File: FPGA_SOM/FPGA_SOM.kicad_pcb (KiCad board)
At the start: 6 copper layers, 49 x 47.1 mm, 64 parts, among them J1 Conn_01x12, J2 Conn_02x05_Counter_Clockwise, J3 Conn_01x06, J5 Conn_01x02, J7 Conn_01x09, J8 Conn_01x10, SW1 SW_Push, U1 ICE40UP5K-SG48ITR, U2 AP2127N-3.3, U3 AP2127N-1.2, U4 W25X20CLSN, X1 ECS-2520MV-xxx-xx

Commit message: QOL changes before production.
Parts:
- removed the ? at (147.2, 112.8) (x2)
- removed the ? at (147.5, 140.8)
- removed D2, D3, D4: LED_Small, Diode_SMD:D_0603_1608Metric_Pad1.05x0.95mm_HandSolder
- removed TP5: FSS, TestPoint:TestPoint_THTPad_D2.0mm_Drill1.0mm
- removed TP6: ISS, TestPoint:TestPoint_THTPad_D2.0mm_Drill1.0mm
- added ?: , , F.Cu at (197.2, 98.8)
- added ?: , , F.Cu at (158.5, 62.1)
- added ?: , , B.Cu at (197.2, 98.8)
- added ?: , , B.Cu at (197.2, 70.9)
- added ?: , , B.Cu at (158.5, 62.1)
- added D1: LED_RAGB, LED_SMD:LED_SK6812_EC15_1.5x1.5mm, F.Cu at (182.4, 70.5)
- added R14: 2k2, Resistor_SMD:R_0603_1608Metric, F.Cu at (183.9, 75.8)
- added R15: 2k2, Resistor_SMD:R_0603_1608Metric, F.Cu at (182.4, 75.8)
- added R16: 2k2, Resistor_SMD:R_0603_1608Metric, F.Cu at (180.6, 75.8)
- C17, C7: footprint Capacitor_SMD:C_0805_2012Metric -> Capacitor_SMD:C_0603_1608Metric
- FB1: footprint Resistor_SMD:R_1206_3216Metric -> Resistor_SMD:R_0603_1608Metric
- X1: value ECS-2520MV-xxx-xx -> SX2M20.000B10F20TNN
- moved REF** 85.2 mm to (197.1, 71.5)
- moved R11 68.4 mm to (167.3, 91.7)
- moved FB1 65.7 mm to (172.1, 71.4)
- moved C17 65.3 mm to (172.1, 73.5)
- moved C1 65.2 mm to (180.6, 81.5)
- moved C2 65.2 mm to (180.6, 81.5)
- moved C3 65.2 mm to (177.1, 88.6)
- moved J1 65.2 mm to (189.6, 62.2)
- moved J5 65.2 mm to (170.1, 89.0)
- moved R6 65.2 mm to (173.4, 91.1)
- moved TP9 65.2 mm to (167.8, 96.8)
- moved C12 65.2 mm to (168.5, 82.3)
- moved C18 65.2 mm to (175.5, 71.3)
- moved C20 65.2 mm to (177.0, 93.1)
- moved C5 65.2 mm to (168.5, 80.3)
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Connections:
- REF** pad 1: GND -> /3V3
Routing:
- net +5V: track 7.72 -> 14.9 mm, vias 0 -> 3
- net /ICE_SS: track 15.1 -> 9.36 mm
- net Net-(D1-GK): track 0.00 -> 5.20 mm
- net Net-(D1-BK): track 0.00 -> 4.65 mm
- net Net-(D1-RK): track 0.00 -> 4.51 mm
- net /FLASH_SS: track 23.5 -> 20.1 mm
- net /3V3: track 14.9 -> 13.4 mm, vias 23 -> 21
- net /3: track 22.6 -> 23.8 mm
- net /11: track 23.7 -> 23.0 mm, vias 1 -> 0
- net GND: vias 160 -> 94
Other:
- board text added: "JLCJLCJLCJLC"
- board text added: "NCGND 3V3 CDN ~{CRST} NC SCK FDI FDO FSS"
- board text removed: "Git Repo"
- board text removed: "NC GND 3V3 CDN ~{CRST} NC SCK FDI FDO FSS"

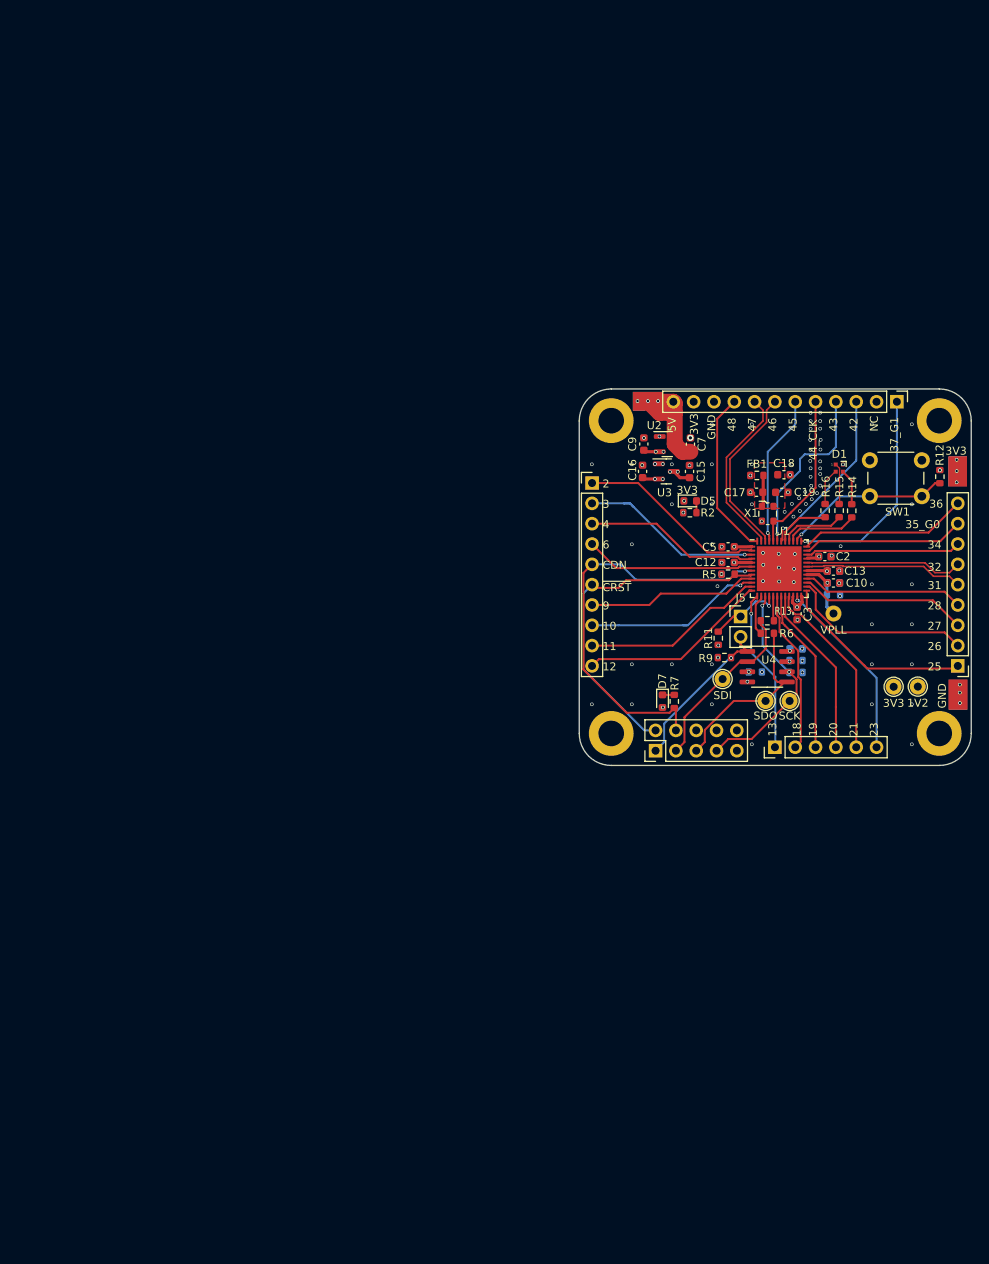
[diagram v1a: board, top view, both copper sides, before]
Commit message: Added ethernet, usb-c, capacitive touch button, and PMOD to schematic. Started PCB layout for V3.
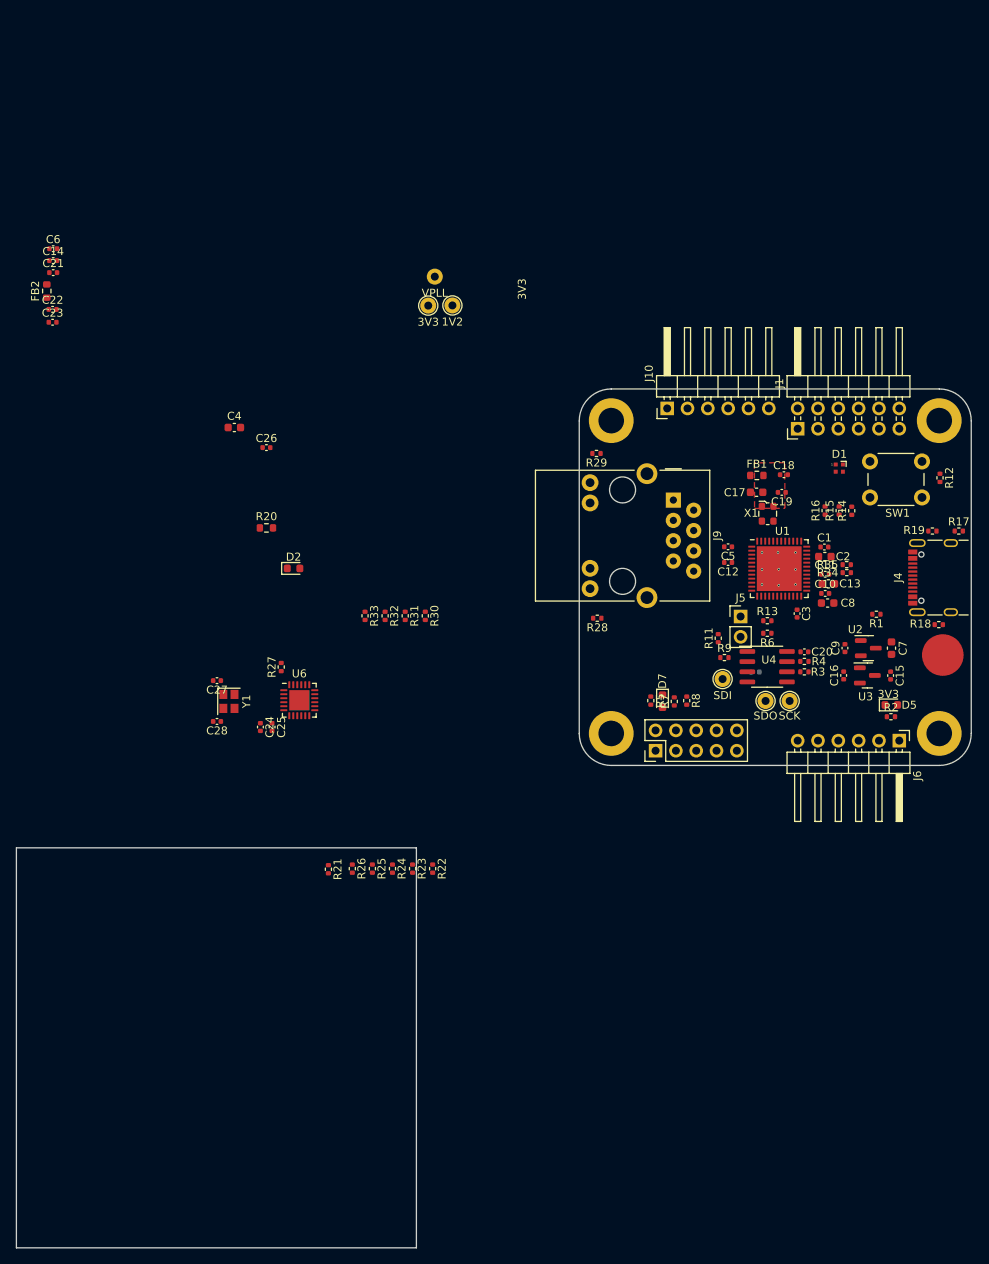
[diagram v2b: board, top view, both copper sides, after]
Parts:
- removed ? (x5): , 
- removed J3: Conn_01x06, Connector_PinHeader_2.54mm:PinHeader_1x06_P2.54mm_Vertical
- removed J7: Conn_01x09, Connector_PinHeader_2.54mm:PinHeader_1x09_P2.54mm_Vertical
- removed J8: Conn_01x10, Connector_PinHeader_2.54mm:PinHeader_1x10_P2.54mm_Vertical
- removed REF**: TestPoint_Pad_2.5x2.5mm, TestPoint:TestPoint_Pad_2.5x2.5mm
- added C14: 100n, Capacitor_SMD:C_0402_1005Metric, F.Cu at (84.1, 44.5)
- added C21: 1u, Capacitor_SMD:C_0402_1005Metric, F.Cu at (84.1, 46.0)
- added C22: 100n, Capacitor_SMD:C_0402_1005Metric, F.Cu at (84.1, 50.6)
- added C23: 1u, Capacitor_SMD:C_0402_1005Metric, F.Cu at (84.1, 52.2)
- added C24: 470p, Capacitor_SMD:C_0402_1005Metric, F.Cu at (110.0, 102.8)
- added C25: 1u, Capacitor_SMD:C_0402_1005Metric, F.Cu at (111.5, 102.8)
- added C26: 1u, Capacitor_SMD:C_0402_1005Metric, F.Cu at (110.8, 67.9)
- added C27: 27p, Capacitor_SMD:C_0402_1005Metric, F.Cu at (104.6, 97.0)
- added C28: 27p, Capacitor_SMD:C_0402_1005Metric, F.Cu at (104.6, 102.1)
- added C4: 10u, Capacitor_SMD:C_0603_1608Metric, F.Cu at (106.8, 65.4)
- added C6: 100n, Capacitor_SMD:C_0402_1005Metric, F.Cu at (84.1, 43.0)
- added D2: D_Schottky, Diode_SMD:D_0603_1608Metric, F.Cu at (114.2, 83.0)
- added FB2: FerriteBead, Resistor_SMD:R_0603_1608Metric, F.Cu at (83.3, 48.3)
- added J10: Conn_01x06, Connector_PinHeader_2.54mm:PinHeader_1x06_P2.54mm_Horizontal, F.Cu at (160.9, 63.0)
- added J4: USB_C_Receptacle_USB2.0, Connector_USB:USB_C_Receptacle_GCT_USB4105-xx-A_16P_TopMnt_Horizontal, F.Cu at (195.3, 84.2)
- added J6: Conn_01x06, Connector_PinHeader_2.54mm:PinHeader_1x06_P2.54mm_Horizontal, F.Cu at (189.9, 104.5)
- added J9: RJ45_Bel_SI-60062-F, Connector_RJ:RJ45_Bel_SI-60062-F, F.Cu at (161.6, 74.5)
- added R17: 0, Resistor_SMD:R_0402_1005Metric, F.Cu at (197.3, 78.3)
- added R18: 5k1, Resistor_SMD:R_0402_1005Metric, F.Cu at (194.8, 90.0)
- added R19: 5k1, Resistor_SMD:R_0402_1005Metric, F.Cu at (194.0, 78.3)
- added R20: 1M, Resistor_SMD:R_0603_1608Metric, F.Cu at (110.8, 77.9)
- added R21: 1K, Resistor_SMD:R_0402_1005Metric, F.Cu at (118.5, 120.6)
- added R22: 10K, Resistor_SMD:R_0402_1005Metric, F.Cu at (131.6, 120.5)
- added R23: 10K, Resistor_SMD:R_0402_1005Metric, F.Cu at (129.0, 120.5)
- added R24: 10K, Resistor_SMD:R_0402_1005Metric, F.Cu at (126.5, 120.5)
- added R25: 10K, Resistor_SMD:R_0402_1005Metric, F.Cu at (124.0, 120.5)
- added R26: 10K, Resistor_SMD:R_0402_1005Metric, F.Cu at (121.5, 120.5)
- added R27: 12K1, Resistor_SMD:R_0402_1005Metric, F.Cu at (112.6, 95.3)
- added R28: 2K2, Resistor_SMD:R_0402_1005Metric, F.Cu at (152.1, 89.2)
- added R29: 2K2, Resistor_SMD:R_0402_1005Metric, F.Cu at (152.0, 68.6)
- added R30: 50, Resistor_SMD:R_0402_1005Metric, F.Cu at (130.6, 88.9)
- added R31: 50, Resistor_SMD:R_0402_1005Metric, F.Cu at (128.1, 88.9)
- added R32: 50, Resistor_SMD:R_0402_1005Metric, F.Cu at (125.6, 88.9)
- added R33: 50, Resistor_SMD:R_0402_1005Metric, F.Cu at (123.1, 88.9)
- added R34: 27, Resistor_SMD:R_0402_1005Metric, F.Cu at (183.3, 83.5)
- added R35: 27, Resistor_SMD:R_0402_1005Metric, F.Cu at (183.3, 82.5)
- added U5: ~, ACustomFootprintLib:Capacitive_touchpad, F.Cu at (195.3, 93.8)
- added U6: LAN8720A, Package_DFN_QFN:VQFN-24-1EP_4x4mm_P0.5mm_EP2.5x2.5mm_ThermalVias, F.Cu at (114.9, 99.5)
- added Y1: 25 MHz, Crystal:Crystal_SMD_2520-4Pin_2.5x2.0mm, F.Cu at (106.1, 99.6)
- C1, C11, C20: footprint Capacitor_SMD:C_0603_1608Metric -> Capacitor_SMD:C_0402_1005Metric; moved to F.Cu
- C10, C12, C15, C16, C18, C19, C3, C5, C9: footprint Capacitor_SMD:C_0603_1608Metric -> Capacitor_SMD:C_0402_1005Metric
- C8: moved to F.Cu
- J1: value Conn_01x12 -> Conn_02x06_Top_Bottom; footprint Connector_PinHeader_2.54mm:PinHeader_1x12_P2.54mm_Vertical -> Connector_PinHeader_2.54mm:PinHeader_2x06_P2.54mm_Horizontal
- R1, R3, R4, R8: footprint Resistor_SMD:R_0603_1608Metric -> Resistor_SMD:R_0402_1005Metric; moved to F.Cu
- R10, R11, R12, R13, R14, R15, R16, R2, R5, R6, R7, R9: footprint Resistor_SMD:R_0603_1608Metric -> Resistor_SMD:R_0402_1005Metric
- U4: value W25X20CLSN -> W25Q128JVSIQ
- moved TP3 75.2 mm to (131.0, 50.1)
- moved TP4 75.2 mm to (134.0, 50.1)
- moved TP1 65.2 mm to (131.8, 46.5)
- moved C9 35.8 mm to (183.1, 93.0)
- moved C15 35.8 mm to (188.8, 96.4)
- moved C16 35.8 mm to (182.9, 96.4)
- moved R2 35.8 mm to (188.8, 101.5)
- moved C7 35.8 mm to (188.9, 93.0)
- moved D5 35.8 mm to (188.9, 100.1)
- moved U2 35.8 mm to (186.0, 93.0)
- moved U3 35.8 mm to (185.9, 96.4)
- moved R5 18.5 mm to (158.8, 99.5), turned to -90 degrees
- moved R8 16.6 mm to (163.3, 99.5), turned to -90 degrees
- moved J1 12.8 mm to (177.2, 65.5), turned to 90 degrees
- moved R1 5.89 mm to (187.0, 88.7), turned to 180 degrees
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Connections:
- J1 pad 1: /37_G1 -> /45
- J1 pad 12: +5V -> /3V3
- J1 pad 2: /38 -> /46
- J1 pad 5: /CLK_IN_G6 -> /36
- J1 pad 6: /45 -> /37_G1
- J1 pad 7: /DP1_N -> /34
- J1 pad 8: /DP1_P -> /35_G0
- J1 pad 9: /48 -> GND
- U1 pad 10: /10 -> /ETH_TXD1
- U1 pad 11: /11 -> /ETH_MDIO
- U1 pad 12: /12 -> /ETH_MDC
- U1 pad 13: /13 -> /ETH_CRSDV
- U1 pad 18: /18 -> /ETH_~{INT}
- U1 pad 19: /19 -> /ETH_RXD1
- U1 pad 20: /20 -> /ETH_RXD0
- U1 pad 21: /21 -> /ETH_RXER
- U1 pad 28: /28 -> /Cap_touch
- U1 pad 3: /3 -> /ETH_~{RST}
- U1 pad 31: /RDP_N -> /D_N
- U1 pad 32: /RDP_P -> /D_P
- U1 pad 46: /DP1_N -> /46
- U1 pad 47: /DP1_P -> /47
- U1 pad 6: /6 -> /ETH_TXEN
- U1 pad 9: /9 -> /ETH_TXD0
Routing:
- net /CDONE: track 51.7 -> 0.00 mm, vias 1 -> 0
- net /CRESET: track 44.5 -> 0.00 mm
- net /SCK: track 27.2 -> 0.00 mm, vias 2 -> 0
- net /37_G1: track 26.7 -> 0.00 mm, vias 1 -> 0
- net /25: track 24.5 -> 0.00 mm
- net /12: track 24.2 -> 0.00 mm
- net /3: track 23.8 -> 0.00 mm, vias 1 -> 0
- net /2: track 23.7 -> 0.00 mm
- net /FLASH_DI: track 23.2 -> 0.00 mm
- net /26: track 23.2 -> 0.00 mm
- net /23: track 23.1 -> 0.00 mm, vias 1 -> 0
- net /11: track 23.0 -> 0.00 mm
- net /21: track 22.8 -> 0.00 mm
- net /10: track 22.6 -> 0.00 mm, vias 1 -> 0
- net /43: track 22.2 -> 0.00 mm, vias 1 -> 0
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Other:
- board size 49 x 47.1 mm -> 119.4 x 107.4 mm
- board text removed: "10"
- board text removed: "11"
- board text removed: "12"
- board text removed: "13"
- board text removed: "18"
- board text removed: "19"
- board text removed: "2"
- board text removed: "20"
- board text removed: "21"
- board text removed: "23"
- board text removed: "25"
- board text removed: "26"
- board text removed: "27"
- board text removed: "28"
- board text removed: "3"
- board text removed: "31"
- board text removed: "32"
- board text removed: "34"
- board text removed: "35_G0"
- board text removed: "36"
- board text removed: "37_G1"
- board text removed: "4"
- board text removed: "42"
- board text removed: "43"
- board text removed: "44_CLK"
- board text removed: "45"
- board text removed: "46"
- board text removed: "47"
- board text removed: "48"
- board text removed: "5V"
- board text removed: "6"
- board text removed: "9"
- board text removed: "CDN"
- board text removed: "GND"
- board text removed: "NC"
- board text removed: "~{CRST}"

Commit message: V3. New form factor, many improvements.
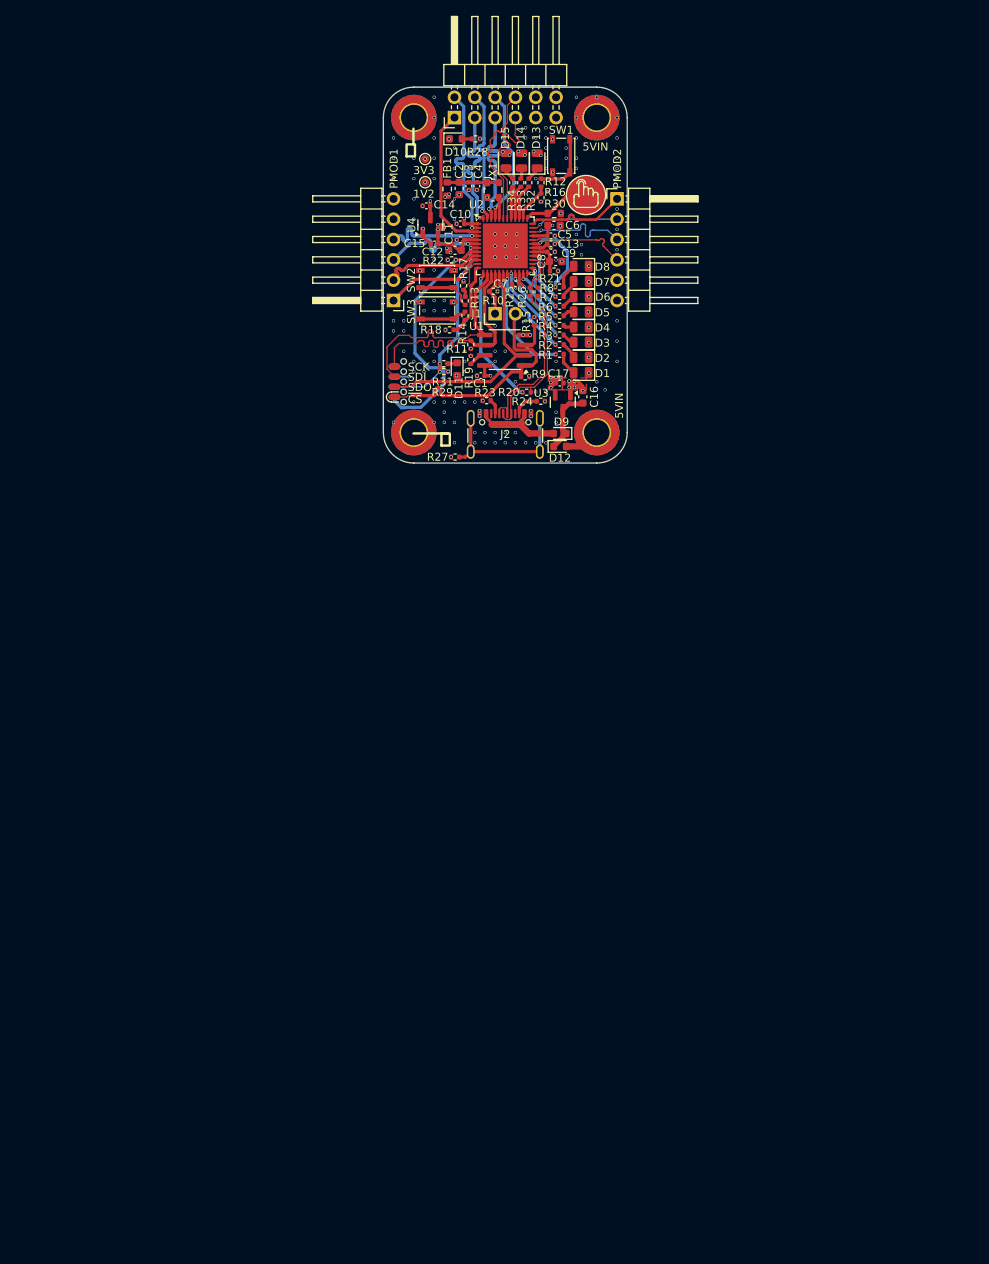
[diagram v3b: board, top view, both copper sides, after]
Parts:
- removed C18, C20, C22: 100n, Capacitor_SMD:C_0402_1005Metric
- removed C19: 10n, Capacitor_SMD:C_0402_1005Metric
- removed C21, C23, C25, C26: 1u, Capacitor_SMD:C_0402_1005Metric
- removed C24: 470p, Capacitor_SMD:C_0402_1005Metric
- removed C27, C28: 27p, Capacitor_SMD:C_0402_1005Metric
- removed FB2: FerriteBead, Resistor_SMD:R_0603_1608Metric
- removed J10: Conn_01x06, Connector_PinHeader_2.54mm:PinHeader_1x06_P2.54mm_Horizontal
- removed J9: RJ45_Bel_SI-60062-F, Connector_RJ:RJ45_Bel_SI-60062-F
- removed R35: 27, Resistor_SMD:R_0402_1005Metric
- removed TP3: 3V3, TestPoint:TestPoint_THTPad_D2.0mm_Drill1.0mm
- removed TP4: 1V2, TestPoint:TestPoint_THTPad_D2.0mm_Drill1.0mm
- removed TP7: SCK, TestPoint:TestPoint_THTPad_D2.0mm_Drill1.0mm
- removed TP8: SDO, TestPoint:TestPoint_THTPad_D2.0mm_Drill1.0mm
- removed TP9: SDI, TestPoint:TestPoint_THTPad_D2.0mm_Drill1.0mm
- removed U6: LAN8720A, Package_DFN_QFN:VQFN-24-1EP_4x4mm_P0.5mm_EP2.5x2.5mm_ThermalVias
- removed Y1: 25 MHz, Crystal:Crystal_SMD_2520-4Pin_2.5x2.0mm
- added D10: LED, Diode_SMD:D_0603_1608Metric, F.Cu at (134.4, 29.3)
- added D11: LED, Diode_SMD:D_0603_1608Metric, F.Cu at (134.6, 58.1)
- added D12: D_Schottky, Diode_SMD:D_0603_1608Metric, F.Cu at (147.5, 67.8)
- added D13: RLED, LED_SMD:LED_0805_2012Metric, F.Cu at (144.6, 32.0)
- added D14: GLED, LED_SMD:LED_0805_2012Metric, F.Cu at (142.7, 32.0)
- added D15: BLED, LED_SMD:LED_0805_2012Metric, F.Cu at (140.7, 32.0)
- added D3: BLED, LED_SMD:LED_0805_2012Metric, F.Cu at (150.1, 54.7)
- added D4: BLED, LED_SMD:LED_0805_2012Metric, F.Cu at (150.1, 52.8)
- added D6: YLED, LED_SMD:LED_0805_2012Metric, F.Cu at (150.1, 49.0)
- added D8: RLED, LED_SMD:LED_0805_2012Metric, F.Cu at (150.1, 45.2)
- added D9: D_Schottky, Diode_SMD:D_0603_1608Metric, F.Cu at (147.5, 66.1)
- added J3: Conn_02x06_Top_Bottom, Connector_PinHeader_2.54mm:PinHeader_2x06_P2.54mm_Horizontal, F.Cu at (134.3, 26.6)
- added SW2: SW_Push, Button_Switch_SMD:SW_SPST_PTS810, F.Cu at (132.1, 46.8)
- added SW3: SW_Push, Button_Switch_SMD:SW_SPST_PTS810, F.Cu at (132.1, 50.8)
- added TP2: 1V2, TestPoint:TestPoint_Pad_D1.0mm, F.Cu at (130.6, 34.7)
- C12, C6: value 100n -> 4.7u; footprint Capacitor_SMD:C_0402_1005Metric -> Capacitor_SMD:C_0603_1608Metric
- C13: value 4.7u -> 100n; footprint Capacitor_SMD:C_0603_1608Metric -> Capacitor_SMD:C_0402_1005Metric
- C14: value 100n -> 1u
- C16: value 1u -> 10u; footprint Capacitor_SMD:C_0402_1005Metric -> Capacitor_SMD:C_0603_1608Metric
- C17: value 10u -> 1u; footprint Capacitor_SMD:C_0603_1608Metric -> Capacitor_SMD:C_0402_1005Metric
- C2: value 4.7u -> 10u
- C4: value 10u -> 10n; footprint Capacitor_SMD:C_0603_1608Metric -> Capacitor_SMD:C_0402_1005Metric
- C7: value 10u -> 100n; footprint Capacitor_SMD:C_0603_1608Metric -> Capacitor_SMD:C_0402_1005Metric
- C9: value 1u -> 100n
- D1: value LED_RAGB -> GLED; footprint LED_SMD:LED_SK6812_EC15_1.5x1.5mm -> LED_SMD:LED_0805_2012Metric
- D2: value D_Schottky -> GLED; footprint Diode_SMD:D_0603_1608Metric -> LED_SMD:LED_0805_2012Metric
- D5: value LED -> YLED; footprint Diode_SMD:D_0603_1608Metric -> LED_SMD:LED_0805_2012Metric
- D7: value LED -> RLED; footprint Diode_SMD:D_0603_1608Metric -> LED_SMD:LED_0805_2012Metric
- H1, H2, H3, H4: value MountingHole -> MountingHole_Pad; footprint MountingHole:MountingHole_3.2mm_M3_DIN965_Pad -> MountingHole:MountingHole_3.2mm_M3_ISO7380_Pad_TopBottom
- J1: value Conn_02x06_Top_Bottom -> Conn_01x02; footprint Connector_PinHeader_2.54mm:PinHeader_2x06_P2.54mm_Horizontal -> Connector_PinHeader_2.54mm:PinHeader_1x02_P2.54mm_Vertical
- J2: value Conn_02x05_Counter_Clockwise -> USB_C_Receptacle_USB2.0; footprint Connector_PinHeader_2.54mm:PinHeader_2x05_P2.54mm_Vertical -> Connector_USB:USB_C_Receptacle_GCT_USB4105-xx-A_16P_TopMnt_Horizontal
- J4: value USB_C_Receptacle_USB2.0 -> Conn_02x04_Counter_Clockwise; footprint Connector_USB:USB_C_Receptacle_GCT_USB4105-xx-A_16P_TopMnt_Horizontal -> ACustomFootprintLib:SOIC_clipProgSmall
- J5: value Conn_01x02 -> Conn_01x06; footprint Connector_PinHeader_2.54mm:PinHeader_1x02_P2.54mm_Vertical -> Connector_PinHeader_2.54mm:PinHeader_1x06_P2.54mm_Horizontal
- R1: value 100 -> 470
- R10: moved to F.Cu
- R12: value 10k -> 1k
- R13: value 0 -> 1k
- R14, R7: value 2k2 -> 1k
- R15, R16: value 2k2 -> 10k
- R17: value 0 -> 10k
- R18, R19: value 5k1 -> 10k
- R2: value 2k2 -> 470
- R20: value 1M -> 1k5; footprint Resistor_SMD:R_0603_1608Metric -> Resistor_SMD:R_0402_1005Metric
- R21: value 1K -> 100
- R22: value 10K -> 10k
- R23, R24: value 10K -> 5k1
- R25, R26: value 10K -> 68
- R27: value 12K1 -> 0
- R28: value 2K2 -> 2k2
- R29: value 2K2 -> 4k7
- R3, R4, R5: value 10k -> 470
- R30: value 50 -> 1M; footprint Resistor_SMD:R_0402_1005Metric -> Resistor_SMD:R_0603_1608Metric
- R31, R32, R33: value 50 -> 2k2
- R34: value 27 -> 2k2
- R6: value 0 -> 470
- R8: value 4k7 -> 1k
- SW1: footprint Button_Switch_THT:SW_PUSH_6mm -> Button_Switch_SMD:SW_SPST_PTS810
- TP1: value VPLL -> 3V3; footprint TestPoint:TestPoint_THTPad_D2.0mm_Drill1.0mm -> TestPoint:TestPoint_Pad_D1.0mm; moved to F.Cu
- U1: value ICE40UP5K-SG48ITR -> W25Q128JVSIQ; footprint Package_DFN_QFN:QFN-48-1EP_7x7mm_P0.5mm_EP5.6x5.6mm -> Package_SO:SOIC-8_3.9x4.9mm_P1.27mm
- U2: value AP2127N-3.3 -> ICE40UP5K-SG48ITR; footprint Package_TO_SOT_SMD:SOT-23 -> Package_DFN_QFN:QFN-48-1EP_7x7mm_P0.5mm_EP5.6x5.6mm
- U3: value AP2127N-1.2 -> AP2127N-3.3
- U4: value W25Q128JVSIQ -> AP2127N-1.2; footprint Package_SO:SOIC-8_3.9x4.9mm_P1.27mm -> Package_TO_SOT_SMD:SOT-23
- X1: value SX2M20.000B10F20TNN -> SX2M36.000B10F20TNN
- moved H3 101.2 mm to (129.2, 26.6)
- moved R21 79.9 mm to (146.7, 45.8), turned to 0 degrees
- moved C15 78.5 mm to (131.8, 42.5), turned to 180 degrees
- moved J6 76.4 mm to (154.6, 36.8), turned to 0 degrees
- moved R22 76.1 mm to (133.9, 44.4), turned to 0 degrees
- moved R26 75.7 mm to (144.7, 48.4), turned to 90 degrees
- moved R25 74.7 mm to (143.7, 48.4), turned to 90 degrees
- moved J4 73.4 mm to (126.0, 59.7), turned to -90 degrees
- moved U5 72.8 mm to (150.7, 36.3), turned to 90 degrees
- moved R18 71.4 mm to (133.7, 53.2), turned to 0 degrees
- moved U4 69.4 mm to (131.3, 40.1), turned to 90 degrees
- moved R17 69.1 mm to (135.4, 47.7), turned to -90 degrees
- moved U2 67.7 mm to (140.6, 42.7)
- moved C3 67.4 mm to (136.1, 35.2)
- moved C7 65.4 mm to (141.9, 47.4), turned to 180 degrees
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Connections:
- C10 pad 1: /VCCPLL -> /3V3
- C14 pad 1: /ETH_3V3 -> GND
- C14 pad 2: GND -> /3V3
- C15 pad 1: GND -> /1V2
- C15 pad 2: /3V3 -> GND
- C16 pad 1: /1V2 -> GND
- C16 pad 2: GND -> +5V
- C17 pad 1: /V_OSC -> /3V3
- C2 pad 1: /3V3 -> /V_OSC
- C3 pad 1: /3V3 -> /V_OSC
- C4 pad 1: +5V -> GND
- C4 pad 2: GND -> /V_OSC
- C6 pad 1: /ETH_3V3 -> /3V3
- C7 pad 1: GND -> /3V3
- C7 pad 2: +5V -> GND
- C9 pad 1: /3V3 -> /VCCPLL
- D1 pad 1: Net-(D1-RK) -> GND
- D1 pad 2: /3V3 -> Net-(D1-A)
- D2 pad 1: +5V -> GND
- D7 pad 1: Net-(D7-K) -> GND
- D7 pad 2: /3V3 -> Net-(D7-A)
- H1 pad 1: (no net) -> Net-(D12-A)
- H2 pad 1: (no net) -> Net-(D12-A)
- H3 pad 1: (no net) -> GND
- H4 pad 1: (no net) -> GND
- J1 pad 1: /45 -> /ICE_SS
- J1 pad 2: /46 -> /FLASH_SS
- J5 pad 1: /ICE_SS -> /PMOD1_28
- J5 pad 2: /FLASH_SS -> /PMOD1_26
- J6 pad 1: /27 -> /PMOD3_36
- J6 pad 2: /26 -> /PMOD3_35_G0
- J6 pad 3: /25 -> /PMOD3_34
- J6 pad 4: /23 -> /PMOD3_32
- R1 pad 1: /VCCPLL -> Net-(D1-A)
- R1 pad 2: /1V2 -> /GLED0
- R10 pad 2: Net-(U4-~{WP}) -> /ICE_SS
- R11 pad 2: /ICE_SS -> /SCK
- R12 pad 1: GND -> /31_button
- R12 pad 2: /38_button -> Net-(R12-Pad2)
- R13 pad 1: /FLASH_DO -> /Button_2
- R13 pad 2: Net-(U1B-IOB_33b_SPI_SI) -> Net-(R13-Pad2)
- R14 pad 1: /RGB0 -> /Button_6
- R14 pad 2: Net-(D1-RK) -> Net-(R14-Pad2)
- R15 pad 1: /RGB1 -> /3V3
- R15 pad 2: Net-(D1-GK) -> Net-(U1-~{WP})
- R16 pad 1: /RGB2 -> GND
- R16 pad 2: Net-(D1-BK) -> /31_button
- R17 pad 1: Net-(J4-SHIELD) -> GND
- R17 pad 2: GND -> /Button_2
- R18 pad 1: Net-(J4-CC1) -> GND
- R18 pad 2: GND -> /Button_6
- R19 pad 1: Net-(J4-CC2) -> /3V3
- R19 pad 2: GND -> Net-(U1-~{HOLD})
- R2 pad 1: /3V3 -> Net-(D2-A)
- R2 pad 2: Net-(D5-A) -> /GLED1
- R20 pad 1: +3V3 -> /Din_P
- R20 pad 2: /Cap_touch -> /USB_Detect
- R21 pad 1: /3V3 -> /VCCPLL
- R21 pad 2: /ETH_MDIO -> /1V2
- R22 pad 2: /ETH_CRSDV -> /CRESET
- R23 pad 1: /3V3 -> Net-(J2-CC1)
- R23 pad 2: /ETH_RXER -> GND
- R24 pad 1: /3V3 -> Net-(J2-CC2)
- R24 pad 2: /ETH_RXD1 -> GND
- R25 pad 1: /3V3 -> /Din_N
- R25 pad 2: /ETH_RXD0 -> /D_N
- R26 pad 1: /3V3 -> /Din_P
- R26 pad 2: /ETH_~{RST} -> /D_P
- R27 pad 1: /RBIAS -> Net-(J2-SHIELD)
- R28 pad 1: /LED1/REGOFF -> /3V3
- R29 pad 1: /LED2/~{INTSEL} -> /3V3
- R29 pad 2: Net-(J9-LEDY_A) -> /CDONE
- R3 pad 1: /3V3 -> Net-(D3-A)
- R3 pad 2: /SCK -> /BLED0
- R30 pad 1: /ETH_3V3 -> /3V3
- R30 pad 2: /TXP -> /Cap_touch
- R31 pad 1: /ETH_3V3 -> /CDONE
- R31 pad 2: /TXN -> Net-(D11-K)
- R32 pad 1: /ETH_3V3 -> /RGB0
- R32 pad 2: /RXP -> Net-(D13-K)
- R33 pad 1: /ETH_3V3 -> /RGB1
- R33 pad 2: /RXN -> Net-(D14-K)
- R34 pad 1: Net-(J4-D--PadA7) -> /RGB2
- R34 pad 2: /D_N -> Net-(D15-K)
- R4 pad 1: /3V3 -> Net-(D4-A)
- R4 pad 2: Net-(U4-~{HOLD}) -> /BLED1
- R5 pad 1: /3V3 -> Net-(D5-A)
- R5 pad 2: /CRESET -> /YLED0
- R6 pad 1: /FLASH_DI -> Net-(D6-A)
- R6 pad 2: Net-(U1B-IOB_32a_SPI_SO) -> /YLED1
- R7 pad 1: /CDONE -> Net-(D7-A)
- R7 pad 2: Net-(D7-K) -> /RLED0
- R8 pad 1: /3V3 -> Net-(D8-A)
- R8 pad 2: /CDONE -> /RLED1
- SW1 pad 2: /38_button -> Net-(R12-Pad2)
- TP1 pad 1: /VCCPLL -> /3V3
- U1 pad 1: /3V3 -> /FLASH_SS
- U1 pad 2: /2 -> /FLASH_DO
- U1 pad 3: /ETH_~{RST} -> Net-(U1-~{WP})
- U1 pad 4: /4 -> GND
- U1 pad 5: /1V2 -> /FLASH_DI
- U1 pad 6: /ETH_TXEN -> /SCK
- U1 pad 7: /CDONE -> Net-(U1-~{HOLD})
- U1 pad 8: /CRESET -> /3V3
- U2 pad 1: GND -> /3V3
- U2 pad 2: /3V3 -> /PMOD2_47
- U2 pad 3: +5V -> /PMOD2_48
- U3 pad 2: /1V2 -> /3V3
- U3 pad 3: /3V3 -> +5V
- U4 pad 1: /FLASH_SS -> GND
- U4 pad 2: /FLASH_DO -> /1V2
- U4 pad 3: Net-(U4-~{WP}) -> /3V3
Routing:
- net Net-(D12-A): track 0.00 -> 46.3 mm, vias 0 -> 3
- net /CRESET: track 0.00 -> 31.5 mm, vias 0 -> 1
- net /FLASH_SS: track 0.00 -> 30.8 mm
- net /FLASH_DO: track 0.00 -> 30.0 mm
- net /SCK: track 0.00 -> 29.8 mm
- net /FLASH_DI: track 0.00 -> 27.6 mm
- net /CDONE: track 0.00 -> 24.4 mm, vias 0 -> 3
- net Net-(D9-A): track 0.00 -> 22.1 mm
- net /Din_P: track 0.00 -> 21.2 mm
- net /Din_N: track 0.00 -> 20.7 mm
- net /3V3: track 0.00 -> 19.7 mm, vias 0 -> 36
- net /PMOD2_47: track 0.00 -> 19.5 mm, vias 0 -> 1
- net Net-(J2-SHIELD): track 0.00 -> 18.7 mm
- net /PMOD3_37_G1: track 0.00 -> 18.5 mm
- net /PMOD2_48: track 0.00 -> 18.4 mm
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- added copper zone on F.Cu, net /3V3
- added copper zone on F.Cu, net GND
- removed copper zone on F.Cu, net /V_OSC
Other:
- board size 119.4 x 107.4 mm -> 30.5 x 47 mm
- board text added: "10"
- board text added: "1V2"
- board text added: "2"
- board text added: "3"
- board text added: "32"
- board text added: "34"
- board text added: "35"
- board text added: "36"
- board text added: "4"
- board text added: "42"
- board text added: "43"
- board text added: "45"
- board text added: "46"
- board text added: "47"
- board text added: "48"
- board text added: "5VIN"
- board text added: "6"
- board text added: "9"
- board text added: "CDN"
- board text added: "FPGA SOM V3 22/12/2024 T. D. McKellar"
- board text added: "GND"
- board text added: "PMOD1"
- board text added: "PMOD2"
- board text added: "SCK"
- board text added: "SDI"
- board text added: "SDO"
- board text added: "X"
- board text added: "~{CS}"
- board text added: "~{RST}"
- board text added: "⏚"
- board text removed: "JLCJLCJLCJLC"
- board text removed: "NCGND 3V3 CDN ~{CRST} NC SCK FDI FDO FSS"
- board text removed: "https://github.com/ Tobi-McKellar/ iCE40UP5k_Breakout"
